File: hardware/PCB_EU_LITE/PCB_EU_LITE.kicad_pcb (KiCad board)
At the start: 4 copper layers, 100 x 100 mm, 165 parts, among them J101 24 V IN, J201 UART 3V3, J301 MEM2061 SPI, J401 SHT4x XH2.54-4P-90, J403 FLOAT / GND, J411 FAN1 2510-4P 90deg, J421 FAN2 2510-4P 90deg, J501 LED + / GND, J701 PTC + / RETURN, J702 PUMP + / RETURN, Q102 IRL2505, Q411 FAN1 AO3422, Q421 FAN2 AO3422, Q501 BSC146N10LS5, Q701 BC847B-DIO, Q702 BC857B, Q703 BSC146N10LS5, Q704 AO3422, Q901 BC847B (R), Q902 BC847B (G), Q903 BC847B (B), SW201 RESET, SW202 BOOT, U101 ST1S14PHR, U102 INA238, U201 ST1S10PHR, U202 ESP32-WROOM-32E-N4, U301 MCP7940N, U401 USBLC6-2SC6, U501 LM3429MH/NOPB, Y301 32.768k CL7p

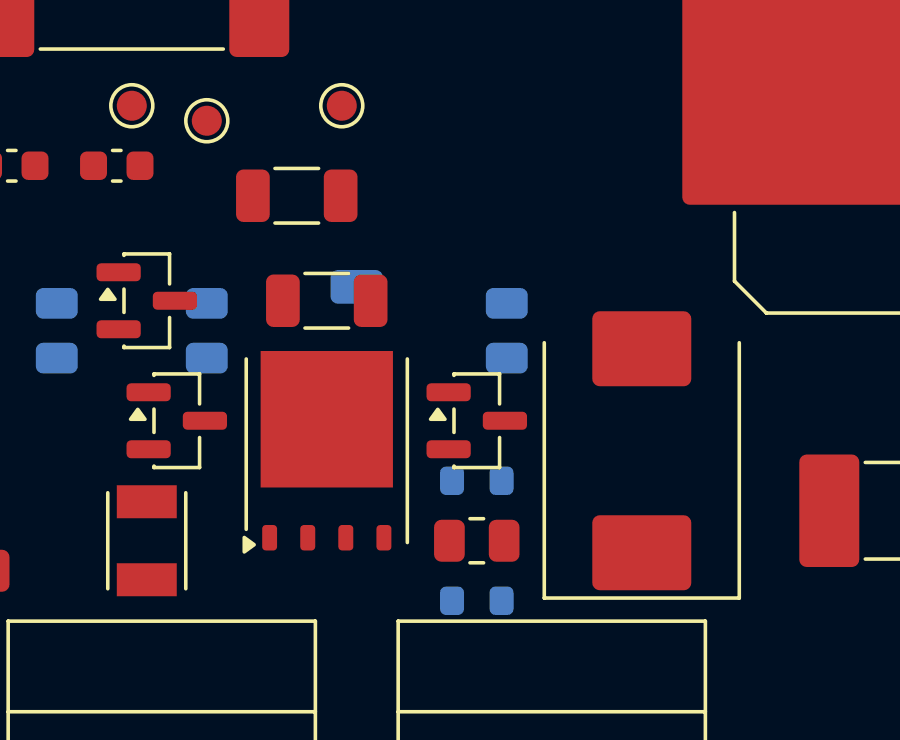
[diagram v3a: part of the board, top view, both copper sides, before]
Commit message: Replace EU-LITE PTC MOSFET with TO-220 part
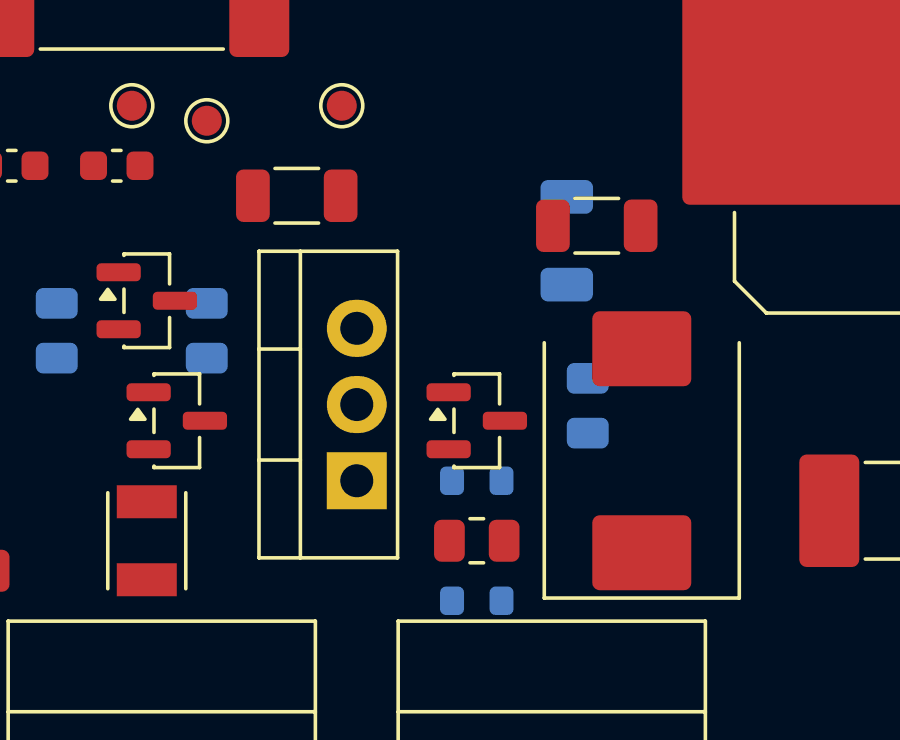
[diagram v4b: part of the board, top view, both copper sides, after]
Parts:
- Q703: value BSC146N10LS5 -> CSD19531KCS; footprint Package_TO_SOT_SMD:TDSON-8-1 -> Package_TO_SOT_THT:TO-220-3_Vertical
- moved R706 9.34 mm to (63.0, 75.5)
- moved R703 7.62 mm to (62.0, 76.0)
- moved R704 3.68 mm to (62.7, 81.5)
- moved Q703 1.41 mm to (55.0, 84.0)
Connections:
- Q703 pad 1: GND -> PTC_GATE
- Q703 pad 2: GND -> PTC_DRAIN

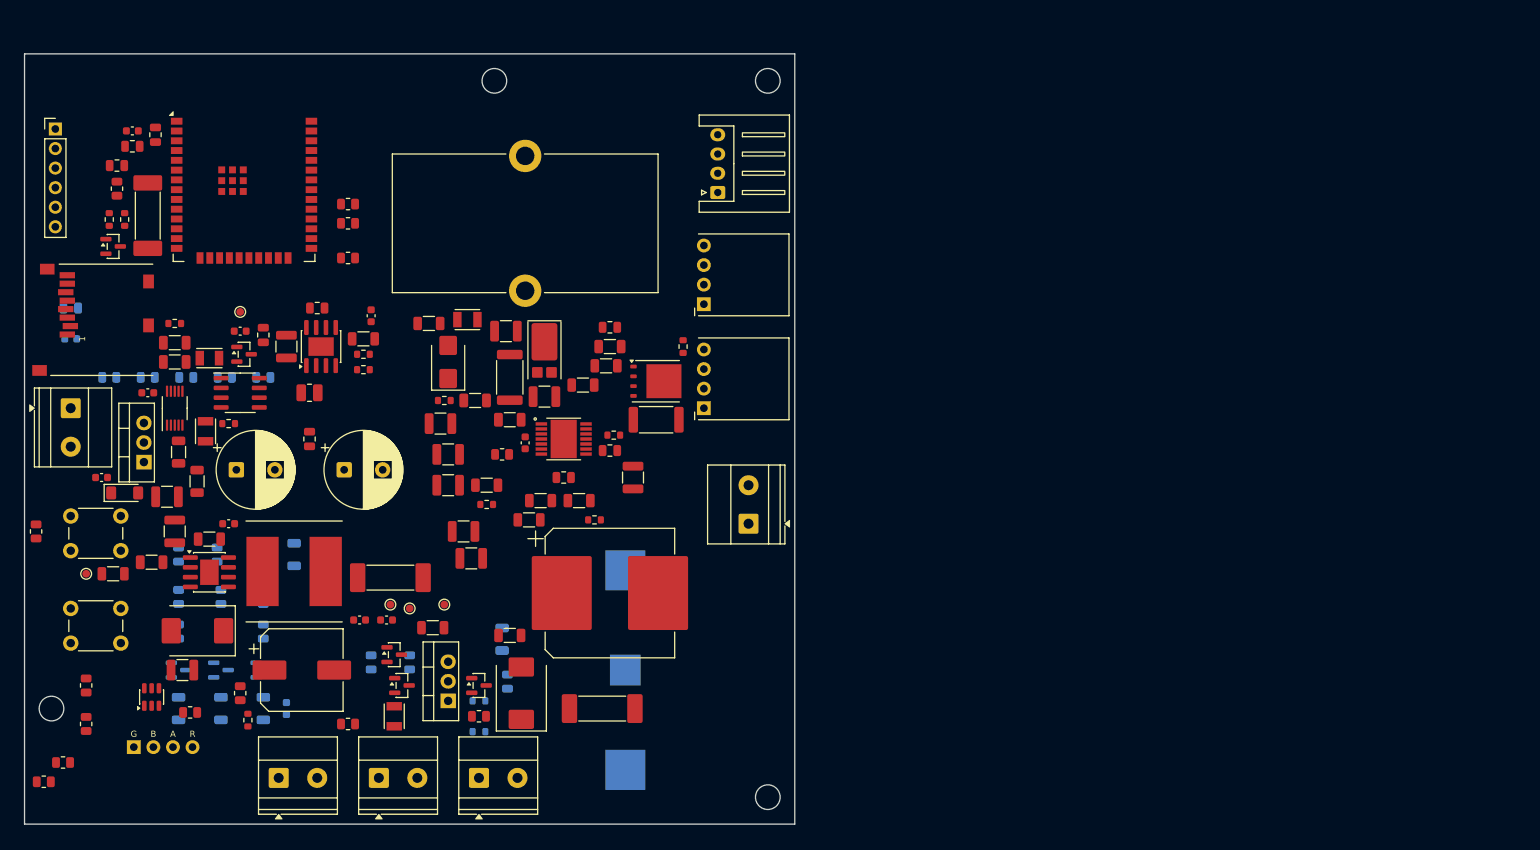
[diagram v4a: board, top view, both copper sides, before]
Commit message: WIP: route EU-LITE power and signal nets
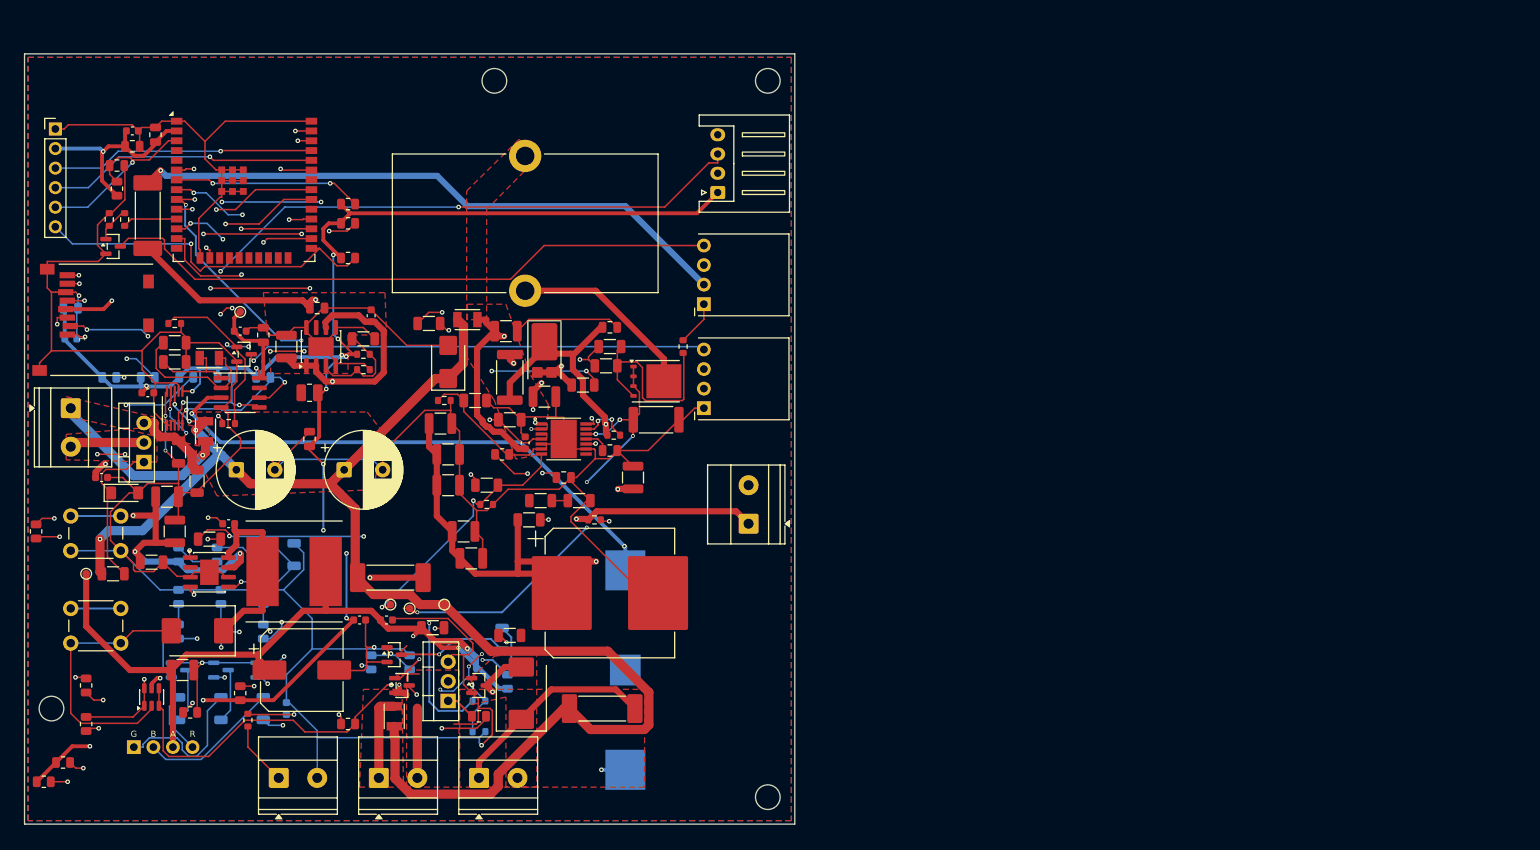
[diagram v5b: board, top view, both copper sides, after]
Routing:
- net GND: track 0.00 -> 753.1 mm, vias 0 -> 6
- net +3V3: track 0.00 -> 312.5 mm, vias 0 -> 17
- net +12V: track 0.00 -> 220.1 mm, vias 0 -> 6
- net +24V_FUSED: track 0.00 -> 192.7 mm, vias 0 -> 4
- net PUMP_GPIO: track 0.00 -> 172.0 mm, vias 0 -> 6
- net SHT_SCL: track 0.00 -> 152.5 mm, vias 0 -> 4
- net SHT_SDA: track 0.00 -> 140.8 mm, vias 0 -> 3
- net I2C_SCL: track 0.00 -> 106.7 mm, vias 0 -> 4
- net VBAT: track 0.00 -> 104.6 mm, vias 0 -> 3
- net ESP_BOOT: track 0.00 -> 104.4 mm, vias 0 -> 1
- net LED_OUT: track 0.00 -> 104.3 mm, vias 0 -> 3
- net I2C_SDA: track 0.00 -> 102.4 mm, vias 0 -> 4
- net +12V_FANS: track 0.00 -> 93.9 mm, vias 0 -> 1
- net SD_CS: track 0.00 -> 92.4 mm, vias 0 -> 4
- net FLOAT_GPIO: track 0.00 -> 91.6 mm, vias 0 -> 3
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- added copper zone on F.Cu, net +12V
- added copper zone on F.Cu, net +24V_FUSED
- added copper zone on F.Cu, net +24V_LED
- added copper zone on F.Cu, net +24V_PTC
- added copper zone on F.Cu, net +24V_PUMP
- added copper zone on F.Cu, net +24V_RAW
- added copper zone on B.Cu, net GND
- added copper zone on F.Cu, net GND
- added copper zone on In1.Cu, net GND
- added copper zone on F.Cu, net PSU_RTN
- added copper zone on F.Cu, net PTC_DRAIN
- added copper zone on F.Cu, net PUMP_DRAIN

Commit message: Route LED CSH and relocate LED bypass cap
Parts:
- C503: moved to B.Cu
- moved C503 4.74 mm to (63.5, 55.0)
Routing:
- net LED_CSH: track 0.00 -> 13.6 mm, vias 0 -> 2
- net GND: track 753.1 -> 766.1 mm, vias 6 -> 7
- net +24V_LED: track 63.7 -> 69.9 mm, vias 4 -> 5

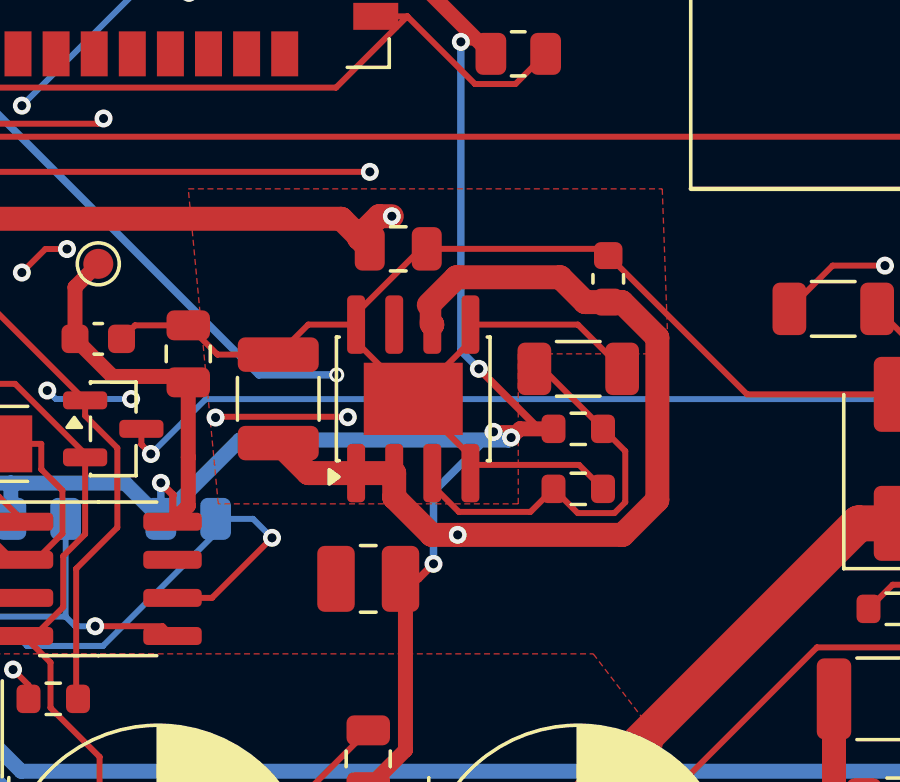
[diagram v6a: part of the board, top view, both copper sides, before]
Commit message: Route EU-LITE logic switch node
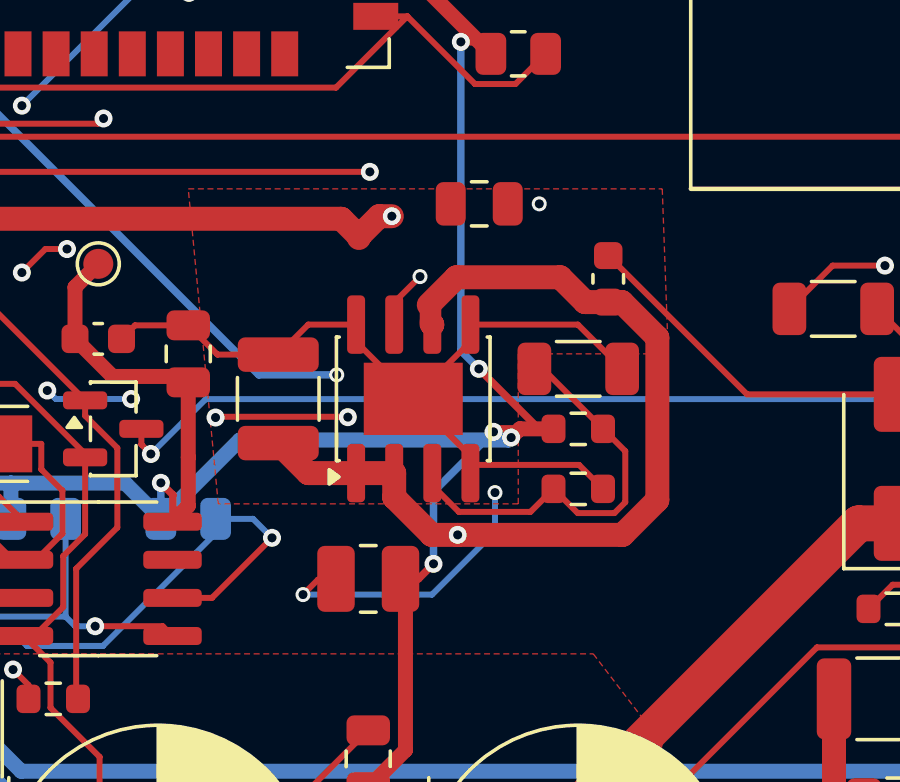
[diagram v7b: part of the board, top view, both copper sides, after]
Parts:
- moved C203 3.09 mm to (40.7, 31.5)
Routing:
- net LOGIC_SW: track 0.00 -> 20.2 mm, vias 0 -> 3
- net GND: track 766.1 -> 756.6 mm, vias 7 -> 8
- net +12V: track 220.1 -> 219.6 mm
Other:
- board text added: "EU-LITE / PARTIALLY ROUTED / 100 x 100 mm / 4 Cu / NOT FOR FABRICATION"
- board text removed: "EU-LITE / UNROUTED / 100 x 100 mm / 4 Cu / NOT FOR FABRICATION"
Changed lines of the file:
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@@
 	(paper "A4")
 	(title_block
-		(title "EU-LITE / unrouted placement")
+		(title "EU-LITE / routing in progress")
 		(date "2026-10-25")
-		(rev "EU-LITE-0.1-PLACEMENT")
+		(rev "EU-LITE-0.1-ROUTING")
 	)
 	(layers
@@
 	(footprint "Capacitor_SMD:C_0805_2012Metric"
 		(layer "F.Cu")
-		(at 38 33)
+		(at 40.7 31.5)
 		(descr "Capacitor SMD 0805 (2012 Metric), square (rectangular) end terminal, IPC-7351 nominal, (Body size source: IPC-SM-782 page 76, https://www.pcb-3d.com/wordpress/wp-content/uploads/ipc-sm-782a_amendment_1_and_2.pdf, https://docs.google.com/spreadsheets/d/1BsfQQcO9C6DZCsRaXUlFlo91Tg2WpOkGARC1WS5S8t0/edit?usp=sharing)")
 		(tags "capacitor")
@@
 			(roundrect_rratio 0.25)
 			(net "GND")
+			(zone_connect 2)
 		)
 		(embedded_fonts no)
@@
 			(roundrect_rratio 0.25)
 			(net "GND")
+			(zone_connect 2)
 		)
 		(pad "3" smd roundrect
@@
 		(layer "Edge.Cuts")
 	)
-	(gr_text "EU-LITE / UNROUTED / 100 x 100 mm / 4 Cu / NOT FOR FABRICATION"
+	(gr_text "EU-LITE / PARTIALLY ROUTED / 100 x 100 mm / 4 Cu / NOT FOR FABRICATION"
 		(at 50 -18 0)
 		(layer "Dwgs.User")
@@
 	)
 	(segment
-		(start 36.6888 32.6388)
-		(end 37.05 33)
-		(width 0.8)
-		(layer "F.Cu")
-		(net "+12V")
-	)
-	(segment
 		(start 13.683 80)
 		(end 8.0013 74.3183)
@@
 	)
 	(segment
-		(start 36.595 35.1572)
-		(end 38.7522 33)
-		(width 0.2)
-		(layer "F.Cu")
-		(net "GND")
-	)
-	(segment
 		(start 80.2183 70)
 		(end 70.9489 60.7306)
@@
 	)
 	(segment
-		(start 36.595 35.525)
-		(end 36.595 35.1572)
-		(width 0.2)
-		(layer "F.Cu")
-		(net "GND")
-	)
-	(segment
 		(start 14.1473 66.968)
 		(end 14.1473 66.1473)
@@
 	)
 	(segment
-		(start 38.7522 33)
-		(end 38.95 33)
-		(width 0.2)
-		(layer "F.Cu")
-		(net "GND")
-	)
-	(segment
 		(start 19.5 60.525)
 		(end 19.975 60.05)
@@
 	)
 	(segment
-		(start 44.775 33)
-		(end 38.95 33)
-		(width 0.2)
-		(layer "F.Cu")
-		(net "GND")
-	)
-	(segment
 		(start 15.2629 38.5491)
 		(end 15.2629 38.4755)
@@
 	)
 	(via
+		(at 42.7 31.5)
+		(size 0.5)
+		(drill 0.3)
+		(layers "F.Cu" "B.Cu")
+		(net "GND")
+	)
+	(via
 		(at 18.3 51.5)
 		(size 0.5)
@@
 	)
 	(segment
+		(start 35.925 44.025)
+		(end 35.925 44)
+		(width 0.2)
+		(layer "F.Cu")
+		(net "LOGIC_SW")
+	)
+	(segment
+		(start 34.825 44.525)
+		(end 35.325 44.025)
+		(width 0.2)
+		(layer "F.Cu")
+		(net "LOGIC_SW")
+	)
+	(segment
+		(start 35.325 44.025)
+		(end 35.925 44.025)
+		(width 0.2)
+		(layer "F.Cu")
+		(net "LOGIC_SW")
+	)
+	(segment
+		(start 37.865 35.525)
+		(end 37.825 35.525)
+		(width 0.2)
+		(layer "F.Cu")
+		(net "LOGIC_SW")
+	)
+	(segment
+		(start 37.825 34.825)
+		(end 38.725 33.925)
+		(width 0.2)
+		(layer "F.Cu")
+		(net "LOGIC_SW")
+	)
+	(segment
+		(start 37.825 35.525)
+		(end 37.825 34.825)
+		(width 0.2)
+		(layer "F.Cu")
+		(net "LOGIC_SW")
+	)
+	(via
+		(at 41.225 41.125)
+		(size 0.5)
+		(drill 0.3)
+		(layers "F.Cu" "B.Cu")
+		(net "LOGIC_SW")
+	)
+	(via
+		(at 38.725 33.925)
+		(size 0.5)
+		(drill 0.3)
+		(layers "F.Cu" "B.Cu")
+		(net "LOGIC_SW")
+	)
+	(via
+		(at 34.825 44.525)
+		(size 0.5)
+		(drill 0.3)
+		(layers "F.Cu" "B.Cu")
+		(net "LOGIC_SW")
+	)
+	(segment
+		(start 41.225 41.125)
+		(end 41.225 42.425)
+		(width 0.2)
+		(layer "B.Cu")
+		(net "LOGIC_SW")
+	)
+	(segment
+		(start 41.225 42.425)
+		(end 39.125 44.525)
+		(width 0.2)
+		(layer "B.Cu")
+		(net "LOGIC_SW")
+	)
+	(segment
+		(start 39.125 44.525)
+		(end 34.825 44.525)
+		(width 0.2)
+		(layer "B.Cu")
+		(net "LOGIC_SW")
+	)
+	(segment
+		(start 38.725 38.625)
+		(end 41.225 41.125)
+		(width 0.2)
+		(layer "In2.Cu")
+		(net "LOGIC_SW")
+	)
+	(segment
+		(start 38.725 33.925)
+		(end 38.725 38.625)
+		(width 0.2)
+		(layer "In2.Cu")
+		(net "LOGIC_SW")
+	)
+	(segment

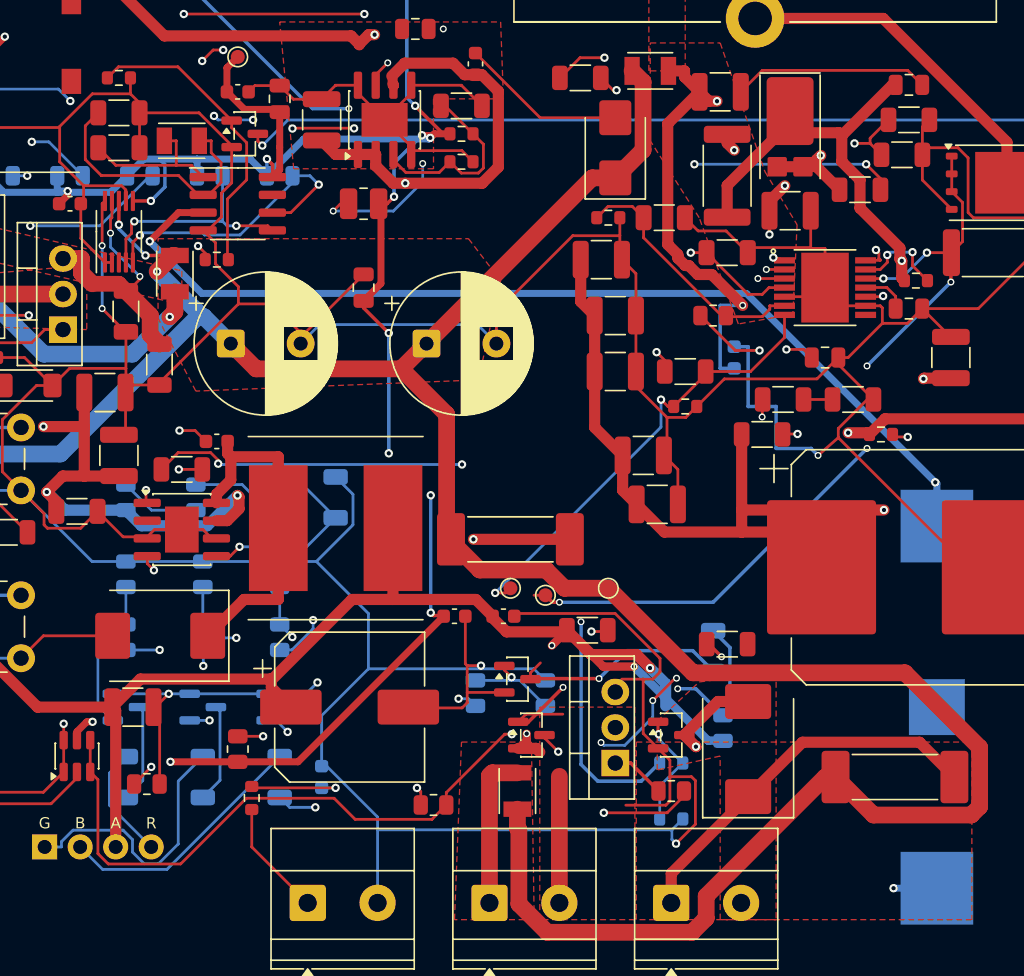
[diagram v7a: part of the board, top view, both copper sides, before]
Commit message: Move and route LITE RTC cluster near battery
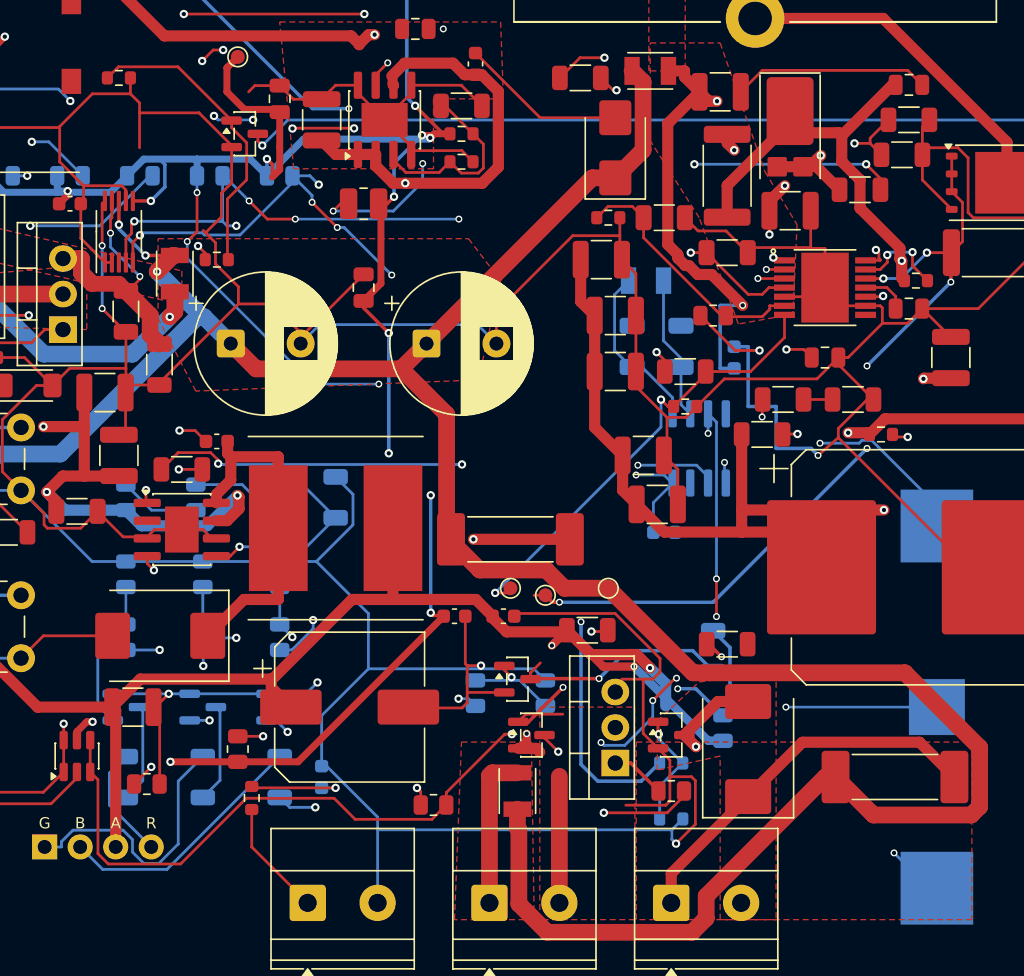
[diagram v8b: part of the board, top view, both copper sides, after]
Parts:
- BT301: footprint EU_Mechanical:Battery_COMF_BC-2001 -> LITE_Mechanical:Battery_COMF_BC-2001
- C301, C302, C303, U301, Y301: moved to B.Cu
- moved C303 43.8 mm to (58.5, 67.5)
- moved C302 43.5 mm to (59.7, 54.2), turned to 90 degrees
- moved C301 39.4 mm to (56.2, 54.2), turned to 90 degrees
- moved U301 37.4 mm to (61.0, 61.5), turned to -90 degrees
- moved Y301 34.7 mm to (57.2, 49.5)
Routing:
- net +3V3: track 312.5 -> 364.2 mm, vias 17 -> 21
- net I2C_SDA: track 102.4 -> 145.7 mm, vias 4 -> 8
- net VBAT: track 104.6 -> 62.7 mm, vias 3 -> 5
- net I2C_SCL: track 106.7 -> 142.0 mm, vias 4 -> 8
- net GND: track 756.6 -> 767.4 mm, vias 8 -> 9
- net RTC_X2: track 19.0 -> 10.5 mm
- net RTC_X1: track 11.0 -> 12.2 mm
